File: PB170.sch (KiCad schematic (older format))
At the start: 14 parts, among them J1 USB_C_Receptacle_USB2.0-Conne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, J2 USB_B_Micro, Q1 P-MOSFET-MLP_HS

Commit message: tiny fixes in annotation
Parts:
- renumbered D1 to D42, R11 to R110, R1 to R42, R9 to R900
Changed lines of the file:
@@
 $EndDescr
 $Comp
-L Device:R R1
+L Device:R R42
 U 1 1 5FCE05A1
 P 1400 3550
-F 0 "R1" H 1470 3596 50  0000 L CNN
+F 0 "R42" H 1470 3596 50  0000 L CNN
 F 1 "220R" H 1470 3505 50  0000 L CNN
 F 2 "Resistors_SMD:R_0603" V 1330 3550 50  0001 C CNN
@@
 $EndComp
 $Comp
-L Device:LED D1
+L Device:LED D42
 U 1 1 5FCE0D28
 P 1400 3850
-F 0 "D1" V 1439 3733 50  0000 R CNN
+F 0 "D42" V 1439 3733 50  0000 R CNN
 F 1 "LED red" V 1348 3733 50  0000 R CNN
 F 2 "LEDs:LED_0603" H 1400 3850 50  0001 C CNN
@@
 $EndComp
 $Comp
-L Device:R R9
+L Device:R R900
 U 1 1 5FCFF67C
 P 1550 2400
-F 0 "R9" H 1620 2446 50  0000 L CNN
+F 0 "R900" H 1620 2446 50  0000 L CNN
 F 1 "10k" H 1620 2355 50  0000 L CNN
 F 2 "Resistors_SMD:R_0603" V 1480 2400 50  0001 C CNN
@@
 	950  950  950  4450
 $Comp
-L Device:R R11
+L Device:R R110
 U 1 1 5FD41C51
 P 1900 6350
-F 0 "R11" H 1970 6396 50  0000 L CNN
+F 0 "R110" H 1970 6396 50  0000 L CNN
 F 1 "220R" H 1970 6305 50  0000 L CNN
 F 2 "Resistors_SMD:R_0603" V 1830 6350 50  0001 C CNN
@@
 Text Notes 4650 900  0    50   ~ 0
 4-bit ALU
-$Comp
-L PB170:USB_C_Receptacle_USB2.0-Connector J1
-U 1 1 5FD02084
-P 1650 6250
-F 0 "J1" H 1757 7117 50  0000 C CNN
-F 1 "USB_C_Receptacle_USB2.0-Connector" H 1757 7026 50  0000 C CNN
-F 2 "PB170:USB_C_Female-16Pin-HPJF" H 1800 6250 50  0001 C CNN
-F 3 "" H 1800 6250 50  0001 C CNN
-	1    1650 6250
-	1    0    0    -1
-$EndComp
 Wire Wire Line
 	1350 7250 1350 7200
@@
 Wire Wire Line
 	6750 3450 7100 3450
+$Comp
+L PB170:USB_C_Receptacle_USB2.0-Connector J1
+U 1 1 5FD02084
+P 1650 6250
+F 0 "J1" H 1757 7117 50  0000 C CNN
+F 1 "USB_C_Receptacle_USB2.0-Connector" H 1757 7026 50  0000 C CNN
+F 2 "PB170:USB_C_Female-16Pin-HPJF" H 1800 6250 50  0001 C CNN
+F 3 "" H 1800 6250 50  0001 C CNN
+	1    1650 6250
+	1    0    0    -1
+$EndComp
 $EndSCHEMATC

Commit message: removed USB C connector
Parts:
- removed J1: USB_C_Receptacle_USB2.0-Connector, PB170:USB_C_Female-16Pin-HPJF, symbol PB170:USB_C_Receptacle_USB2.0-Connector
- renumbered R110 to R43
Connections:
- wire segments 48 -> 36
- no-connect marks 9 -> 5
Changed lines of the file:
@@
 	950  950  950  4450
 $Comp
-L Device:R R110
+L Device:R R43
 U 1 1 5FD41C51
 P 1900 6350
-F 0 "R110" H 1970 6396 50  0000 L CNN
+F 0 "R43" H 1970 6396 50  0000 L CNN
 F 1 "220R" H 1970 6305 50  0000 L CNN
 F 2 "Resistors_SMD:R_0603" V 1830 6350 50  0001 C CNN
@@
 Text Notes 4650 900  0    50   ~ 0
 4-bit ALU
-Wire Wire Line
-	1350 7250 1350 7200
-Wire Wire Line
-	1650 7150 1650 7200
-Wire Wire Line
-	1650 7200 1350 7200
-Connection ~ 1350 7200
-Wire Wire Line
-	1350 7200 1350 7150
-Wire Wire Line
-	2250 5650 2650 5650
-Wire Wire Line
-	2650 5650 2650 5600
-NoConn ~ 2250 5850
-NoConn ~ 2250 5950
-NoConn ~ 2250 6750
-NoConn ~ 2250 6850
-Wire Wire Line
-	2250 6250 2300 6250
-Wire Wire Line
-	2300 6250 2300 6150
-Wire Wire Line
-	2300 6150 2600 6150
-Wire Wire Line
-	2250 6350 2300 6350
-Wire Wire Line
-	2300 6350 2300 6450
-Wire Wire Line
-	2300 6450 2600 6450
 Wire Wire Line
 	2200 2150 2300 2150
@@
 Wire Wire Line
 	6750 3450 7100 3450
-$Comp
-L PB170:USB_C_Receptacle_USB2.0-Connector J1
-U 1 1 5FD02084
-P 1650 6250
-F 0 "J1" H 1757 7117 50  0000 C CNN
-F 1 "USB_C_Receptacle_USB2.0-Connector" H 1757 7026 50  0000 C CNN
-F 2 "PB170:USB_C_Female-16Pin-HPJF" H 1800 6250 50  0001 C CNN
-F 3 "" H 1800 6250 50  0001 C CNN
-	1    1650 6250
-	1    0    0    -1
-$EndComp
 $EndSCHEMATC

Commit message: minor fixes
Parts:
- removed J_PWR1: Conn_01x03, Pin_Headers:Pin_Header_Straight_1x03_Pitch2.54mm, symbol Connector_Generic:Conn_01x03
- removed Q1: P-MOSFET-MLP_HS, PB170:MLP3.3X3.3_HS, symbol PB170:P-MOSFET-MLP_HS
- removed R900: 10k, Resistors_SMD:R_0603, symbol Device:R
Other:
- note removed: "USB supply"
- moved on the sheet: J2, R43
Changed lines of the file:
@@
 $Descr A4 11693 8268
 encoding utf-8
-Sheet 1 9
+Sheet 1 8
 Title ""
 Date ""
@@
 $EndComp
 $Comp
-L Connector_Generic:Conn_01x03 J_PWR1
-U 1 1 5FCE0EDE
-P 2500 2050
-F 0 "J_PWR1" H 2580 2092 50  0000 L CNN
-F 1 "Conn_01x03" H 2580 2001 50  0000 L CNN
-F 2 "Pin_Headers:Pin_Header_Straight_1x03_Pitch2.54mm" H 2500 2050 50  0001 C CNN
-F 3 "~" H 2500 2050 50  0001 C CNN
-	1    2500 2050
-	1    0    0    -1
-$EndComp
-$Comp
-L power:GND #PWR0101
-U 1 1 5FD05268
-P 2200 2150
-F 0 "#PWR0101" H 2200 1900 50  0001 C CNN
-F 1 "GND" V 2205 2022 50  0000 R CNN
-F 2 "" H 2200 2150 50  0001 C CNN
-F 3 "" H 2200 2150 50  0001 C CNN
-	1    2200 2150
-	0    1    1    0
-$EndComp
-$Comp
-L power:GND #PWR0102
-U 1 1 5FD0622F
-P 2200 1950
-F 0 "#PWR0102" H 2200 1700 50  0001 C CNN
-F 1 "GND" V 2205 1822 50  0000 R CNN
-F 2 "" H 2200 1950 50  0001 C CNN
-F 3 "" H 2200 1950 50  0001 C CNN
-	1    2200 1950
-	0    1    1    0
-$EndComp
-$Comp
-L power:+5V #PWR0103
-U 1 1 5FD067D3
-P 1300 2000
-F 0 "#PWR0103" H 1300 1850 50  0001 C CNN
-F 1 "+5V" V 1315 2128 50  0000 L CNN
-F 2 "" H 1300 2000 50  0001 C CNN
-F 3 "" H 1300 2000 50  0001 C CNN
-	1    1300 2000
-	1    0    0    -1
-$EndComp
-Wire Wire Line
-	2200 1950 2300 1950
-$Comp
 L power:GND #PWR0106
 U 1 1 5FD0AF6E
@@
 	2300 3800 2550 3800
 $Comp
-L PB170:P-MOSFET-MLP_HS Q1
-U 1 1 5FCFFF08
-P 1650 2150
-F 0 "Q1" H 1858 2203 59  0000 L CNN
-F 1 "P-MOSFET-MLP_HS" H 1858 2098 59  0000 L CNN
-F 2 "PB170:MLP3.3X3.3_HS" H 1650 2150 50  0001 C CNN
-F 3 "https://datasheet.lcsc.com/szlcsc/Wuxi-NCE-Power-Semiconductor-NCE20P45Q_C193354.pdf" H 1650 2150 50  0001 C CNN
-F 4 "C193354" H 1650 2150 50  0001 C CNN "LCSC"
-	1    1650 2150
-	0    -1   -1   0
-$EndComp
-$Comp
 L Connector:USB_B_Micro J2
 U 1 1 5FD07183
-P 1450 6250
-F 0 "J2" H 1507 6717 50  0000 C CNN
-F 1 "USB_B_Micro" H 1507 6626 50  0000 C CNN
-F 2 "PB170:MICRO-USB-SMD_MICROXNJ" H 1600 6200 50  0001 C CNN
-F 3 "https://datasheet.lcsc.com/szlcsc/1912111437_SHOU-HAN-MicroXNJ_C404969.pdf" H 1600 6200 50  0001 C CNN
-F 4 "C404969" H 1450 6250 50  0001 C CNN "LCSC"
-	1    1450 6250
-	1    0    0    -1
-$EndComp
-$Comp
-L Device:R R900
-U 1 1 5FCFF67C
-P 1550 2400
-F 0 "R900" H 1620 2446 50  0000 L CNN
-F 1 "10k" H 1620 2355 50  0000 L CNN
-F 2 "Resistors_SMD:R_0603" V 1480 2400 50  0001 C CNN
-F 3 "https://datasheet.lcsc.com/szlcsc/Uniroyal-Elec-0603WAF1002T5E_C25804.pdf" H 1550 2400 50  0001 C CNN
-F 4 "C25804" H 1550 2400 50  0001 C CNN "LCSC"
-	1    1550 2400
-	1    0    0    -1
-$EndComp
-$Comp
-L power:GND #PWR0119
-U 1 1 5FCFFB3A
-P 1550 2550
-F 0 "#PWR0119" H 1550 2300 50  0001 C CNN
-F 1 "GND" V 1555 2422 50  0000 R CNN
-F 2 "" H 1550 2550 50  0001 C CNN
-F 3 "" H 1550 2550 50  0001 C CNN
-	1    1550 2550
-	1    0    0    -1
-$EndComp
-Wire Wire Line
-	2300 2050 1850 2050
-Wire Wire Line
-	1450 2050 1300 2050
-Wire Wire Line
-	1300 2050 1300 2000
+P 1400 1750
+F 0 "J2" H 1457 2217 50  0000 C CNN
+F 1 "USB_B_Micro" H 1457 2126 50  0000 C CNN
+F 2 "PB170:MICRO-USB-SMD_MICROXNJ" H 1550 1700 50  0001 C CNN
+F 3 "https://datasheet.lcsc.com/szlcsc/1912111437_SHOU-HAN-MicroXNJ_C404969.pdf" H 1550 1700 50  0001 C CNN
+F 4 "C404969" H 1400 1750 50  0001 C CNN "LCSC"
+	1    1400 1750
+	1    0    0    -1
+$EndComp
 Wire Notes Line
 	950  4450 3250 4450
@@
 L Device:R R43
 U 1 1 5FD41C51
-P 1900 6350
-F 0 "R43" H 1970 6396 50  0000 L CNN
-F 1 "220R" H 1970 6305 50  0000 L CNN
-F 2 "Resistors_SMD:R_0603" V 1830 6350 50  0001 C CNN
-F 3 "https://datasheet.lcsc.com/szlcsc/Uniroyal-Elec-0603WAF2200T5E_C22962.pdf" H 1900 6350 50  0001 C CNN
-F 4 "C22962" H 1900 6350 50  0001 C CNN "LCSC"
-	1    1900 6350
+P 1850 1850
+F 0 "R43" H 1920 1896 50  0000 L CNN
+F 1 "220R" H 1920 1805 50  0000 L CNN
+F 2 "Resistors_SMD:R_0603" V 1780 1850 50  0001 C CNN
+F 3 "https://datasheet.lcsc.com/szlcsc/Uniroyal-Elec-0603WAF2200T5E_C22962.pdf" H 1850 1850 50  0001 C CNN
+F 4 "C22962" H 1850 1850 50  0001 C CNN "LCSC"
+	1    1850 1850
 	0    1    1    0
 $EndComp
 Wire Wire Line
-	1750 6250 2050 6250
-Wire Wire Line
-	2050 6250 2050 6350
+	1700 1750 2000 1750
+Wire Wire Line
+	2000 1750 2000 1850
 $Comp
 L power:GND #PWR0121
 U 1 1 5FD447F1
-P 1350 6750
-F 0 "#PWR0121" H 1350 6500 50  0001 C CNN
-F 1 "GND" H 1355 6577 50  0000 C CNN
-F 2 "" H 1350 6750 50  0001 C CNN
-F 3 "" H 1350 6750 50  0001 C CNN
-	1    1350 6750
-	1    0    0    -1
-$EndComp
-Wire Wire Line
-	1350 6750 1350 6700
-Wire Wire Line
-	1450 6650 1450 6700
-Wire Wire Line
-	1450 6700 1350 6700
-Connection ~ 1350 6700
-Wire Wire Line
-	1350 6700 1350 6650
+P 1300 2250
+F 0 "#PWR0121" H 1300 2000 50  0001 C CNN
+F 1 "GND" H 1305 2077 50  0000 C CNN
+F 2 "" H 1300 2250 50  0001 C CNN
+F 3 "" H 1300 2250 50  0001 C CNN
+	1    1300 2250
+	1    0    0    -1
+$EndComp
+Wire Wire Line
+	1300 2250 1300 2200
+Wire Wire Line
+	1400 2150 1400 2200
+Wire Wire Line
+	1400 2200 1300 2200
+Connection ~ 1300 2200
+Wire Wire Line
+	1300 2200 1300 2150
 $Comp
 L power:+5V #PWR0122
 U 1 1 5FD489FB
-P 1800 6000
-F 0 "#PWR0122" H 1800 5850 50  0001 C CNN
-F 1 "+5V" H 1815 6173 50  0000 C CNN
-F 2 "" H 1800 6000 50  0001 C CNN
-F 3 "" H 1800 6000 50  0001 C CNN
-	1    1800 6000
-	1    0    0    -1
-$EndComp
-Wire Wire Line
-	1750 6050 1800 6050
-Wire Wire Line
-	1800 6050 1800 6000
+P 1750 1500
+F 0 "#PWR0122" H 1750 1350 50  0001 C CNN
+F 1 "+5V" H 1765 1673 50  0000 C CNN
+F 2 "" H 1750 1500 50  0001 C CNN
+F 3 "" H 1750 1500 50  0001 C CNN
+	1    1750 1500
+	1    0    0    -1
+$EndComp
+Wire Wire Line
+	1700 1550 1750 1550
+Wire Wire Line
+	1750 1550 1750 1500
 Wire Notes Line
 	4650 950  4650 4850
@@
 Wire Notes Line
 	10700 950  4650 950
-Wire Notes Line
-	950  5150 950  7550
-Wire Notes Line
-	950  7550 4150 7550
-Wire Notes Line
-	4150 7550 4150 5150
-Wire Notes Line
-	4150 5150 950  5150
-NoConn ~ 1750 6450
+NoConn ~ 1700 1950
 Text Notes 7400 7500 0    50   ~ 0
 Sablona pro zaverecne projekty predmetu PB170 na FI MU Brno
 Text Notes 7050 6700 0    50   ~ 0
 <Jmena autoru>
-Text Notes 950  5100 0    50   ~ 0
-USB supply
 Text Notes 950  900  0    50   ~ 0
 Power management
 Text Notes 4650 900  0    50   ~ 0
 4-bit ALU
-Wire Wire Line
-	2200 2150 2300 2150
 $Comp
 L Mechanical:MountingHole_Pad H1
@@
 NoConn ~ 5150 7300
 $Sheet
-S 6950 5250 1550 850
-U 5FEB4D4D
-F0 "New parts" 50
-F1 "newParts.sch" 50
-$EndSheet
-$Sheet
 S 7100 2150 900  1450

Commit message: Change R, C and LED footprints
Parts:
- C1: footprint Capacitors_SMD:C_0805 -> Capacitor_SMD:C_0805_2012Metric
- C2: footprint Capacitors_SMD:C_0603 -> Capacitor_SMD:C_0805_2012Metric
- D42: footprint LEDs:LED_0603 -> LED_SMD:LED_0603_1608Metric
- R42, R43: footprint Resistors_SMD:R_0603 -> Resistor_SMD:R_0603_1608Metric
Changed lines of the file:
@@
 F 0 "R42" H 1470 3596 50  0000 L CNN
 F 1 "220R" H 1470 3505 50  0000 L CNN
-F 2 "Resistors_SMD:R_0603" V 1330 3550 50  0001 C CNN
+F 2 "Resistor_SMD:R_0603_1608Metric" V 1330 3550 50  0001 C CNN
 F 3 "https://datasheet.lcsc.com/szlcsc/Uniroyal-Elec-0603WAF2200T5E_C22962.pdf" H 1400 3550 50  0001 C CNN
 F 4 "C22962" H 1400 3550 50  0001 C CNN "LCSC"
@@
 F 0 "D42" V 1439 3733 50  0000 R CNN
 F 1 "LED red" V 1348 3733 50  0000 R CNN
-F 2 "LEDs:LED_0603" H 1400 3850 50  0001 C CNN
+F 2 "LED_SMD:LED_0603_1608Metric" H 1400 3850 50  0001 C CNN
 F 3 "https://datasheet.lcsc.com/szlcsc/Hubei-KENTO-Elec-KT-0603R_C2286.pdf" H 1400 3850 50  0001 C CNN
 F 4 "C2286" V 1400 3850 50  0001 C CNN "LCSC"
@@
 F 0 "C1" H 2165 3696 50  0000 L CNN
 F 1 "10uF" H 2165 3605 50  0000 L CNN
-F 2 "Capacitors_SMD:C_0805" H 2088 3500 50  0001 C CNN
+F 2 "Capacitor_SMD:C_0805_2012Metric" H 2088 3500 50  0001 C CNN
 F 3 "https://datasheet.lcsc.com/szlcsc/Samsung-Electro-Mechanics-CL21A106KAYNNNE_C15850.pdf" H 2050 3650 50  0001 C CNN
 F 4 "C15850" H 2050 3650 50  0001 C CNN "LCSC"
@@
 F 0 "C2" H 2665 3696 50  0000 L CNN
 F 1 "100nF" H 2665 3605 50  0000 L CNN
-F 2 "Capacitors_SMD:C_0603" H 2588 3500 50  0001 C CNN
+F 2 "Capacitor_SMD:C_0805_2012Metric" H 2588 3500 50  0001 C CNN
 F 3 "https://datasheet.lcsc.com/szlcsc/YAGEO-CC0603KRX7R9BB104_C14663.pdf" H 2550 3650 50  0001 C CNN
 F 4 "C14663" H 2550 3650 50  0001 C CNN "LCSC"
@@
 F 0 "R43" H 1920 1896 50  0000 L CNN
 F 1 "220R" H 1920 1805 50  0000 L CNN
-F 2 "Resistors_SMD:R_0603" V 1780 1850 50  0001 C CNN
+F 2 "Resistor_SMD:R_0603_1608Metric" V 1780 1850 50  0001 C CNN
 F 3 "https://datasheet.lcsc.com/szlcsc/Uniroyal-Elec-0603WAF2200T5E_C22962.pdf" H 1850 1850 50  0001 C CNN
 F 4 "C22962" H 1850 1850 50  0001 C CNN "LCSC"

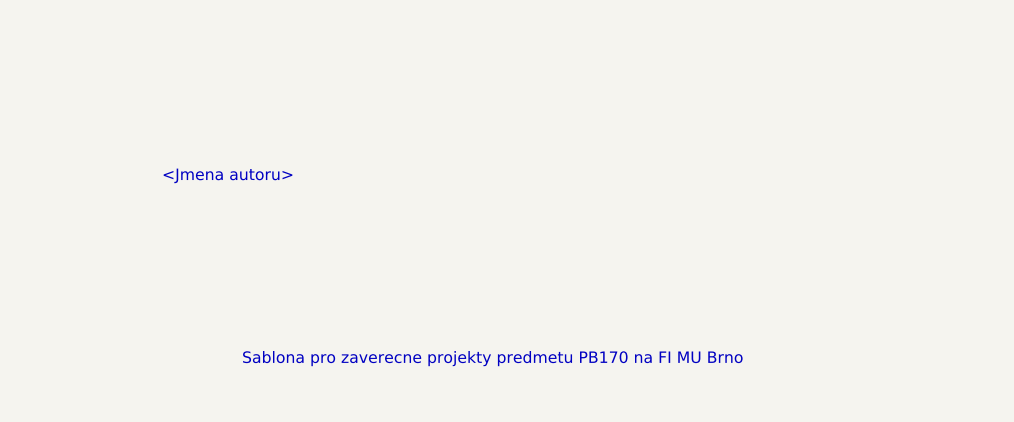
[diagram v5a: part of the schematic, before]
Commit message: Fill main sheet header
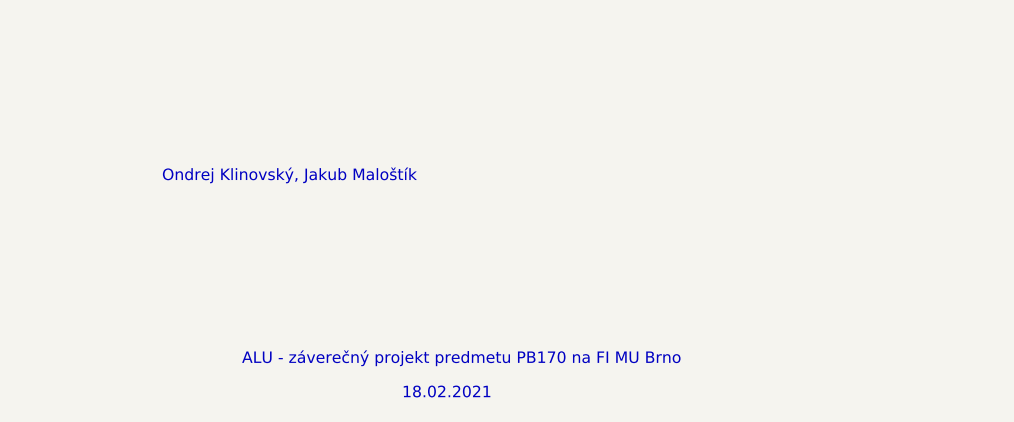
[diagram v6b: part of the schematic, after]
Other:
- note added: "18.02.2021"
- note added: "ALU - záverečný projekt predmetu PB170 na FI MU Brno"
- note added: "Ondrej Klinovský, Jakub Maloštík"
- note removed: "<Jmena autoru>"
- note removed: "Sablona pro zaverecne projekty predmetu PB170 na FI MU Brno"
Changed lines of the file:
@@
 	10700 950  4650 950
 Text Notes 7400 7500 0    50   ~ 0
-Sablona pro zaverecne projekty predmetu PB170 na FI MU Brno
+ALU - záverečný projekt predmetu PB170 na FI MU Brno
 Text Notes 7050 6700 0    50   ~ 0
-<Jmena autoru>
+Ondrej Klinovský, Jakub Maloštík
 Text Notes 950  900  0    50   ~ 0
 Power management
@@
 	1750 1550 1750 1500
 NoConn ~ 1700 1950
+Text Notes 8100 7650 0    50   ~ 0
+18.02.2021
 $EndSCHEMATC
